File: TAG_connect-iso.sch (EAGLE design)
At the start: 9 parts, among them J2 RJ11-6PTH, U2 ISO7231C_DW_16

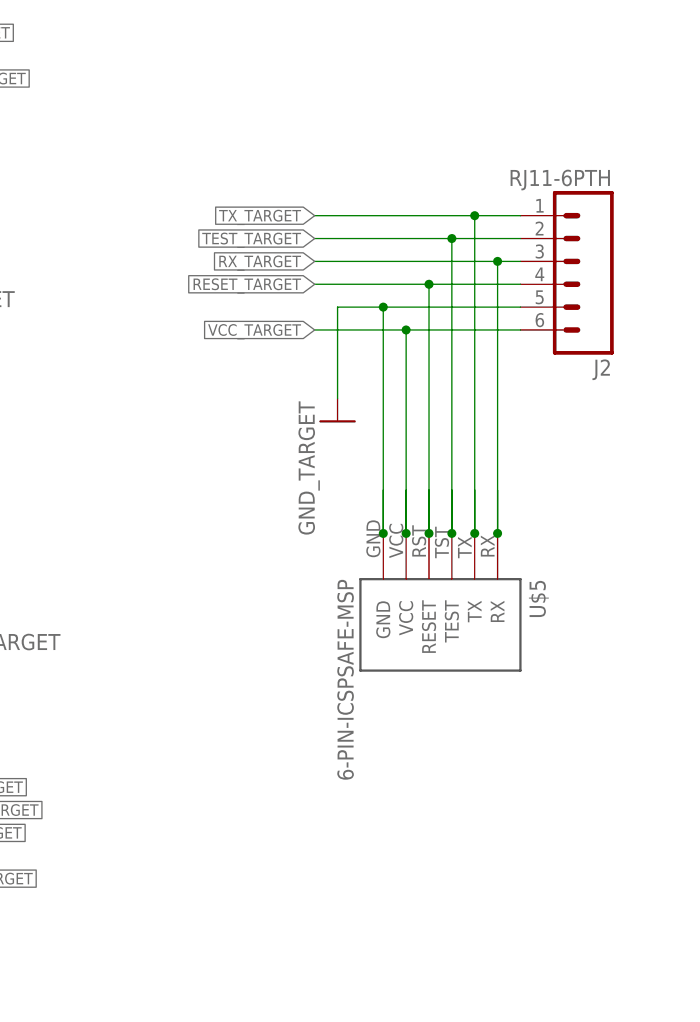
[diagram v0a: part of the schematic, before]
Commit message: bug fixes
updated iso board to new pinout and rj-12 connector
cleaned up safe-msp board
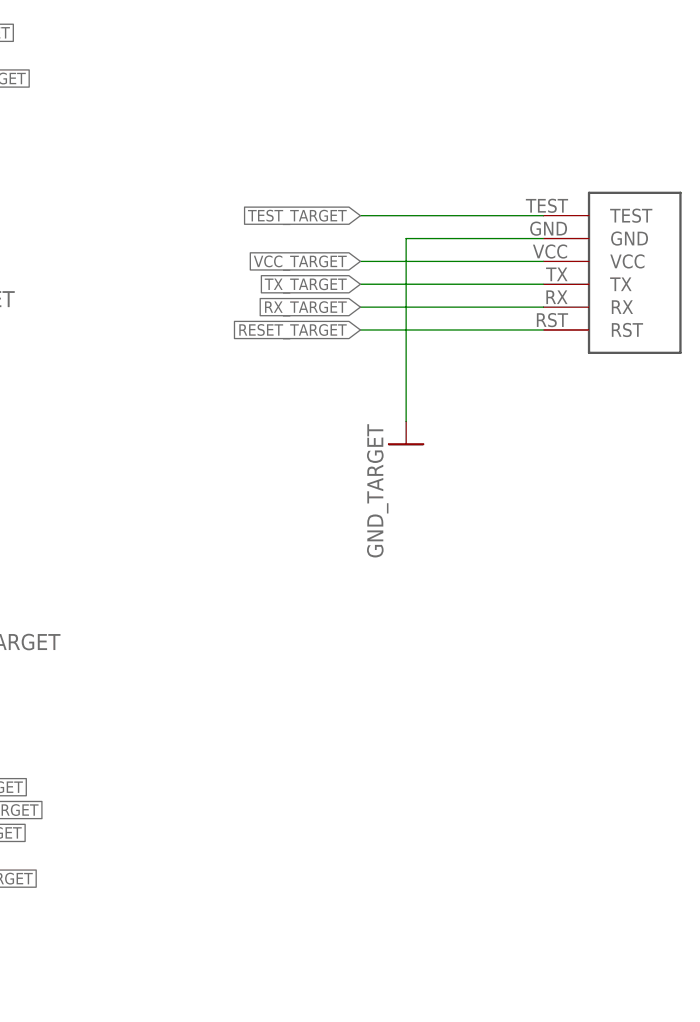
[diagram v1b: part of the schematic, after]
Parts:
- removed J2: RJ11-6PTH, SparkFun-Connectors:RJ11-6PTH
- removed U$5: 6-PIN-ICSPSAFE-MSP, LaunchFET:6-PIN-ICSPSAFE-MSP
- added U$1: RJ-12SMD, LaunchFET:RJ-12SMD
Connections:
- net GND_TARGET: now also U$1.GND; no longer J2.5, U$5.GND
- net RESET_TARGET: now also U$1.RST; no longer J2.4, U$5.RESET
- net RX_TARGET: now also U$1.RX; no longer J2.3, U$5.RX
- net TEST_TARGET: now also U$1.TEST; no longer J2.2, U$5.TEST
- net TX_TARGET: now also U$1.TX; no longer J2.1, U$5.TX
- net VCC_TARGET: now also U$1.VCC; no longer J2.6, U$5.VCC
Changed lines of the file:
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@@
 </classes>
 <parts>
-<part name="J2" library="SparkFun-Connectors" deviceset="RJ11-6" device="PTH"/>
 <part name="JP1" library="SparkFun-Passives" deviceset="JUMPER-2" device="PTH_LOCK"/>
 <part name="U$2" library="TI" deviceset="ISO1540" device=""/>
@@
 <part name="GND1" library="supply1" deviceset="GND" device="" value="GND_TARGET"/>
 <part name="U$4" library="LaunchFET" deviceset="6-PIN-ICSP" device="EASY-MSP"/>
-<part name="U$5" library="LaunchFET" deviceset="6-PIN-ICSP" device="SAFE-MSP"/>
 <part name="GND_FET4" library="supply1" deviceset="GNDA" device="" value="GND_FET"/>
+<part name="U$1" library="LaunchFET" deviceset="RJ-12" device="SMD"/>
 </parts>
 <sheets>
@@
 </plain>
 <instances>
-<instance part="J2" gate="G$1" x="198.12" y="78.74" rot="R180"/>
 <instance part="JP1" gate="A" x="101.6" y="-5.08"/>
 <instance part="U$2" gate="G$1" x="99.06" y="96.52"/>
@@
 <instance part="GND_FET2" gate="1" x="76.2" y="38.1"/>
 <instance part="GND4" gate="1" x="129.54" y="38.1"/>
-<instance part="GND5" gate="1" x="172.72" y="60.96" smashed="yes">
-<attribute name="VALUE" x="170.18" y="48.26" size="1.778" layer="96" rot="R90"/>
+<instance part="GND5" gate="1" x="180.34" y="58.42" smashed="yes">
+<attribute name="VALUE" x="177.8" y="45.72" size="1.778" layer="96" rot="R90"/>
 </instance>
 <instance part="GND_FET3" gate="1" x="83.82" y="-20.32"/>
 <instance part="GND1" gate="1" x="121.92" y="-20.32"/>
 <instance part="U$4" gate="G$1" x="40.64" y="76.2"/>
-<instance part="U$5" gate="G$1" x="182.88" y="38.1" rot="R270"/>
 <instance part="GND_FET4" gate="1" x="20.32" y="58.42"/>
+<instance part="U$1" gate="G$1" x="205.74" y="71.12"/>
 </instances>
 <busses>
@@
 </segment>
 <segment>
-<pinref part="J2" gate="G$1" pin="6"/>
-<wire x1="193.04" y1="71.12" x2="180.34" y2="71.12" width="0.1524" layer="91"/>
-<label x="170.18" y="71.12" size="1.27" layer="95" rot="R180" xref="yes"/>
-<wire x1="180.34" y1="71.12" x2="170.18" y2="71.12" width="0.1524" layer="91"/>
-<wire x1="180.34" y1="53.34" x2="180.34" y2="48.514" width="0.1524" layer="91"/>
-<junction x="180.34" y="71.12"/>
-<pinref part="U$5" gate="G$1" pin="VCC"/>
-<wire x1="180.34" y1="48.514" x2="180.34" y2="71.12" width="0.1524" layer="91"/>
-<junction x="180.34" y="48.514"/>
+<wire x1="195.58" y1="78.74" x2="175.26" y2="78.74" width="0.1524" layer="91"/>
+<label x="175.26" y="78.74" size="1.27" layer="95" rot="R180" xref="yes"/>
+<pinref part="U$1" gate="G$1" pin="VCC"/>
 </segment>
 </net>
@@
 </segment>
 <segment>
-<pinref part="J2" gate="G$1" pin="3"/>
-<wire x1="170.18" y1="78.74" x2="190.5" y2="78.74" width="0.1524" layer="91"/>
-<label x="170.18" y="78.74" size="1.27" layer="95" rot="R180" xref="yes"/>
-<wire x1="190.5" y1="78.74" x2="193.04" y2="78.74" width="0.1524" layer="91"/>
-<wire x1="190.5" y1="53.34" x2="190.5" y2="48.514" width="0.1524" layer="91"/>
-<junction x="190.5" y="78.74"/>
-<pinref part="U$5" gate="G$1" pin="RX"/>
-<wire x1="190.5" y1="48.514" x2="190.5" y2="78.74" width="0.1524" layer="91"/>
-<junction x="190.5" y="48.514"/>
+<wire x1="175.26" y1="73.66" x2="195.58" y2="73.66" width="0.1524" layer="91"/>
+<label x="175.26" y="73.66" size="1.27" layer="95" rot="R180" xref="yes"/>
+<pinref part="U$1" gate="G$1" pin="RX"/>
 </segment>
 </net>
 <net name="TX_TARGET" class="0">
 <segment>
-<pinref part="J2" gate="G$1" pin="1"/>
-<label x="170.18" y="83.82" size="1.27" layer="95" rot="R180" xref="yes"/>
-<wire x1="170.18" y1="83.82" x2="187.96" y2="83.82" width="0.1524" layer="91"/>
-<wire x1="187.96" y1="83.82" x2="193.04" y2="83.82" width="0.1524" layer="91"/>
-<wire x1="187.96" y1="53.34" x2="187.96" y2="48.514" width="0.1524" layer="91"/>
-<junction x="187.96" y="83.82"/>
-<pinref part="U$5" gate="G$1" pin="TX"/>
-<wire x1="187.96" y1="48.514" x2="187.96" y2="83.82" width="0.1524" layer="91"/>
-<junction x="187.96" y="48.514"/>
+<label x="175.26" y="76.2" size="1.27" layer="95" rot="R180" xref="yes"/>
+<wire x1="175.26" y1="76.2" x2="195.58" y2="76.2" width="0.1524" layer="91"/>
+<pinref part="U$1" gate="G$1" pin="TX"/>
 </segment>
 <segment>
@@
 </segment>
 <segment>
-<pinref part="J2" gate="G$1" pin="5"/>
 <pinref part="GND5" gate="1" pin="GND"/>
-<wire x1="172.72" y1="73.66" x2="177.8" y2="73.66" width="0.1524" layer="91"/>
-<wire x1="177.8" y1="73.66" x2="193.04" y2="73.66" width="0.1524" layer="91"/>
-<wire x1="172.72" y1="63.5" x2="172.72" y2="73.66" width="0.1524" layer="91"/>
-<wire x1="177.8" y1="53.34" x2="177.8" y2="48.514" width="0.1524" layer="91"/>
-<junction x="177.8" y="73.66"/>
-<pinref part="U$5" gate="G$1" pin="GND"/>
-<wire x1="177.8" y1="48.514" x2="177.8" y2="73.66" width="0.1524" layer="91"/>
-<junction x="177.8" y="48.514"/>
+<wire x1="180.34" y1="81.28" x2="195.58" y2="81.28" width="0.1524" layer="91"/>
+<wire x1="180.34" y1="60.96" x2="180.34" y2="81.28" width="0.1524" layer="91"/>
+<pinref part="U$1" gate="G$1" pin="GND"/>
 </segment>
 </net>
@@
 <net name="TEST_TARGET" class="0">
 <segment>
-<pinref part="J2" gate="G$1" pin="2"/>
-<label x="170.18" y="81.28" size="1.27" layer="95" rot="R180" xref="yes"/>
-<wire x1="193.04" y1="81.28" x2="185.42" y2="81.28" width="0.1524" layer="91"/>
-<wire x1="185.42" y1="81.28" x2="170.18" y2="81.28" width="0.1524" layer="91"/>
-<wire x1="185.42" y1="53.34" x2="185.42" y2="48.514" width="0.1524" layer="91"/>
-<junction x="185.42" y="81.28"/>
-<pinref part="U$5" gate="G$1" pin="TEST"/>
-<wire x1="185.42" y1="48.514" x2="185.42" y2="81.28" width="0.1524" layer="91"/>
-<junction x="185.42" y="48.514"/>
+<label x="175.26" y="83.82" size="1.27" layer="95" rot="R180" xref="yes"/>
+<wire x1="195.58" y1="83.82" x2="175.26" y2="83.82" width="0.1524" layer="91"/>
+<pinref part="U$1" gate="G$1" pin="TEST"/>
 </segment>
 <segment>
@@
 <net name="RESET_TARGET" class="0">
 <segment>
-<pinref part="J2" gate="G$1" pin="4"/>
-<label x="170.18" y="76.2" size="1.27" layer="95" rot="R180" xref="yes"/>
-<wire x1="170.18" y1="76.2" x2="182.88" y2="76.2" width="0.1524" layer="91"/>
-<wire x1="182.88" y1="76.2" x2="193.04" y2="76.2" width="0.1524" layer="91"/>
-<wire x1="182.88" y1="53.34" x2="182.88" y2="48.514" width="0.1524" layer="91"/>
-<junction x="182.88" y="76.2"/>
-<pinref part="U$5" gate="G$1" pin="RESET"/>
-<wire x1="182.88" y1="48.514" x2="182.88" y2="76.2" width="0.1524" layer="91"/>
-<junction x="182.88" y="48.514"/>
-</segment>
-<segment>
+<label x="175.26" y="71.12" size="1.27" layer="95" rot="R180" xref="yes"/>
+<wire x1="175.26" y1="71.12" x2="195.58" y2="71.12" width="0.1524" layer="91"/>
+<pinref part="U$1" gate="G$1" pin="RST"/>
+</segment>
+<segment>
